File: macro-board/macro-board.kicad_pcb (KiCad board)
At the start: 2 copper layers, 76 parts, among them Q1 Q_NPN_BEC, SW1 SW_Push, U1 ATmega32U2-AU, Y1 16MHz

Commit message: routing pain
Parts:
- C1, C10, C2, C7, C8, C9, D17, D18, D19, D20, D21, F1, R3, R4, R5, R6, USB1, Y1: moved to B.Cu
- R23: value 10k -> 1k
- moved C2 111.9 mm to (125.5, 120.8), turned to 90 degrees
- moved Y1 101.4 mm to (124.4, 125.4)
- moved R8 101.3 mm to (215.3, 51.2)
- moved R12 101.0 mm to (215.0, 60.8)
- moved D16 100.2 mm to (253.4, 93.4), turned to 270 degrees
- moved R18 100.1 mm to (253.4, 88.5), turned to 270 degrees
- moved D14 99.9 mm to (215.3, 93.4), turned to 270 degrees
- moved R14 99.5 mm to (253.2, 61.1)
- moved R16 98.8 mm to (214.5, 88.8), turned to 270 degrees
- moved R10 98.4 mm to (253.2, 50.9)
- moved R20 97.9 mm to (215.1, 98.4)
- moved R22 97.0 mm to (253.2, 98.3)
- moved R1 92.6 mm to (115.4, 124.3), turned to 270 degrees
- moved C6 90.8 mm to (118.0, 129.6), turned to 90 degrees
- moved C5 90.8 mm to (118.0, 134.0)
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
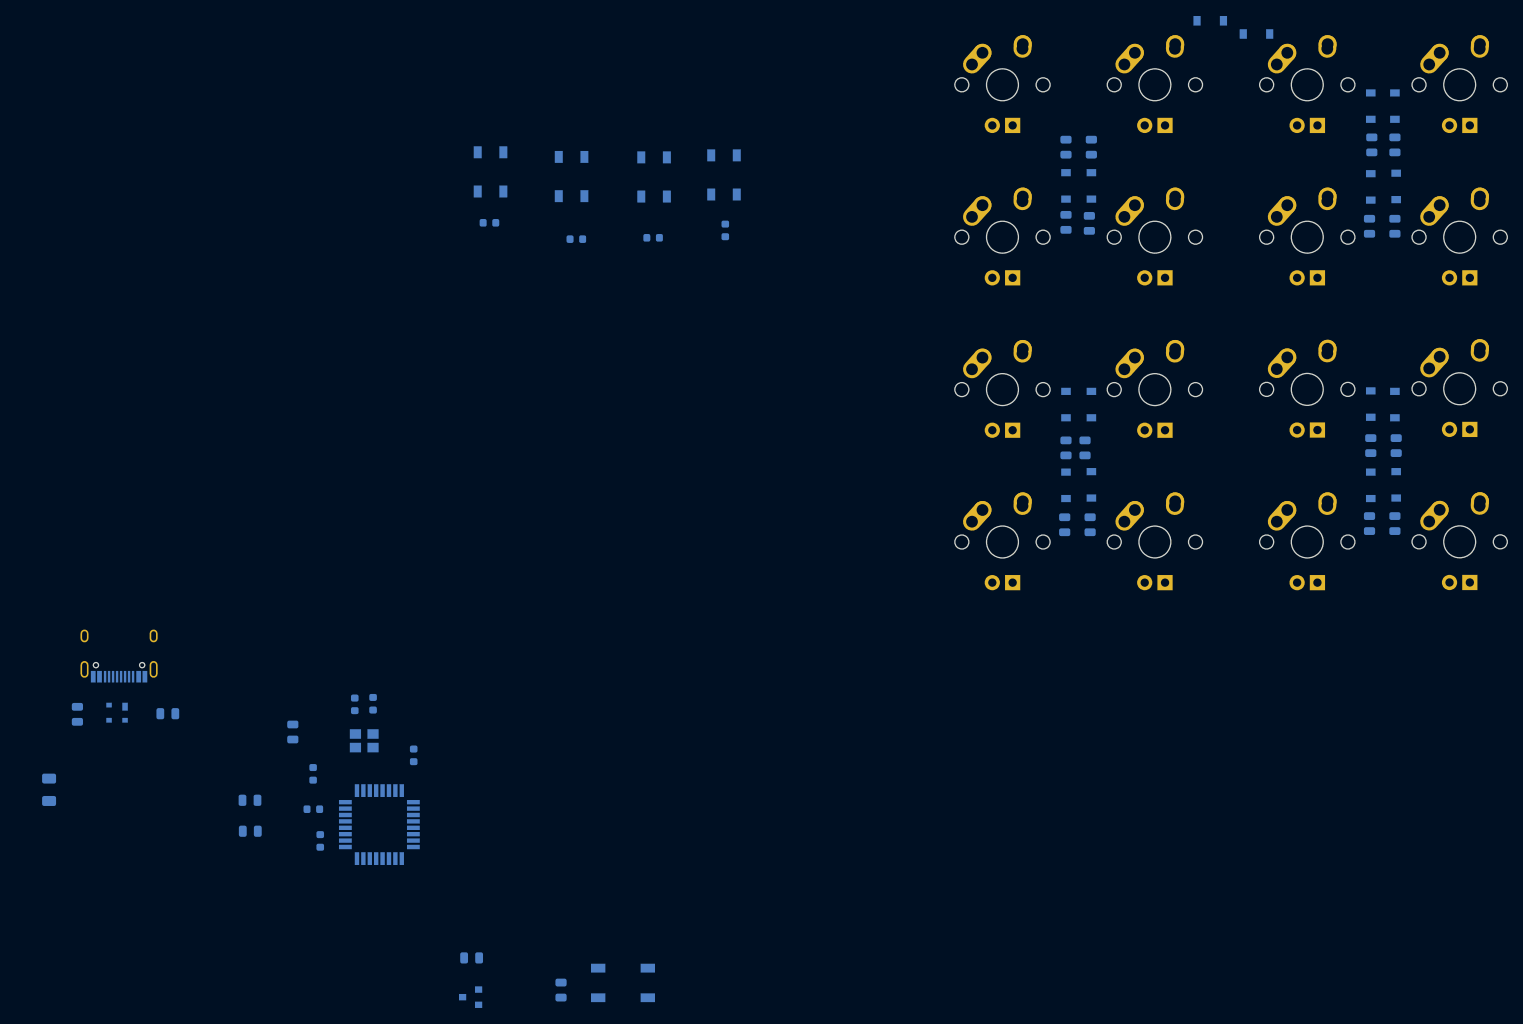
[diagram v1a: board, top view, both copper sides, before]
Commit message: finalize routing
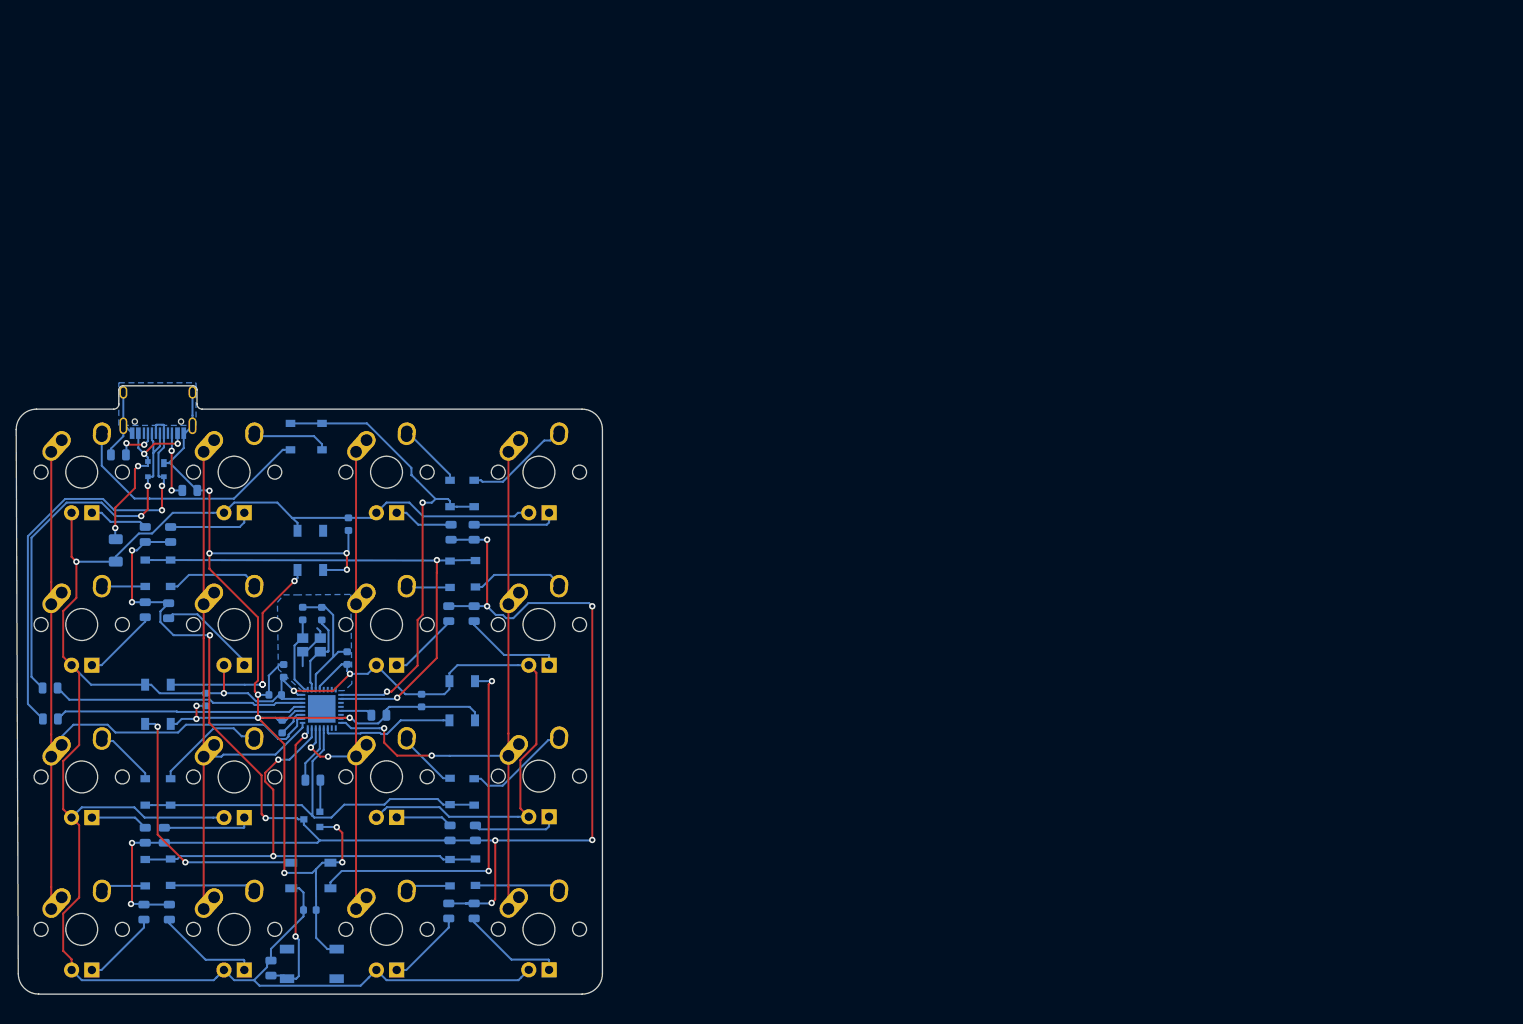
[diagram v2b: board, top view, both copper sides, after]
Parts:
- R2: value 110k -> 10k
- U1: footprint Package_QFP:TQFP-32_7x7mm_P0.8mm -> Housings_DFN_QFN:QFN-32-1EP_5x5mm_Pitch0.5mm
- moved D2 127.2 mm to (119.1, 87.4), turned to 270 degrees
- moved D1 126.2 mm to (115.2, 87.4), turned to 270 degrees
- moved D11 124.9 mm to (135.1, 131.8)
- moved D12 124.9 mm to (138.1, 131.8)
- moved D13 124.9 mm to (97.0, 141.9)
- moved D15 124.9 mm to (135.1, 141.9)
- moved D16 124.9 mm to (138.3, 141.9)
- moved D3 124.9 mm to (135.1, 94.5)
- moved D4 124.9 mm to (138.1, 94.5)
- moved D5 124.9 mm to (97.0, 104.5)
- moved D7 124.9 mm to (135.1, 104.6)
- moved D8 124.9 mm to (138.3, 104.6)
- moved D9 124.9 mm to (97.0, 131.8)
- moved MX1 124.9 mm to (89.1, 91.9)
- moved MX11 124.9 mm to (127.2, 129.9)
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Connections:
- U1 pad 10: Net-(U1-Pad10) -> ROW1
- U1 pad 16: Net-(U1-Pad16) -> COL3
- U1 pad 20: Net-(U1-Pad20) -> ROW2
- U1 pad 22: Net-(U1-Pad22) -> COL2
- U1 pad 23: Net-(U1-Pad23) -> ROW3
- U1 pad 25: Net-(U1-Pad25) -> COL1
- U1 pad 26: Net-(U1-Pad26) -> COL0
- U1 pad 9: Net-(U1-Pad9) -> ROW0
- Y1 pad 2: Net-(Y1-Pad2) -> GND
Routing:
- net +5V: track 0.00 -> 346.1 mm, vias 0 -> 4
- net GND: track 0.00 -> 210.1 mm, vias 0 -> 12
- net LEDGND: track 0.00 -> 206.2 mm, vias 0 -> 12
- net COL0: track 0.00 -> 94.1 mm
- net COL3: track 0.00 -> 80.8 mm, vias 0 -> 2
- net COL1: track 0.00 -> 71.6 mm
- net ROW1: track 0.00 -> 67.6 mm, vias 0 -> 2
- net COL2: track 0.00 -> 66.0 mm, vias 0 -> 2
- net ROW0: track 0.00 -> 61.7 mm, vias 0 -> 2
- net ROW3: track 0.00 -> 61.3 mm, vias 0 -> 2
- net D+: track 0.00 -> 56.5 mm, vias 0 -> 2
- net ROW2: track 0.00 -> 54.6 mm
- net D-: track 0.00 -> 49.8 mm, vias 0 -> 2
- net Net-(D17-Pad2): track 0.00 -> 47.1 mm, vias 0 -> 2
- net Net-(R2-Pad2): track 0.00 -> 35.8 mm, vias 0 -> 2
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- added copper zone on B.Cu, net GND
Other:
- board outline added: 73.3 x 76 mm
- board text added: "Micro Mark 0"
